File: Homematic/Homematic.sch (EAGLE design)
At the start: 26 parts, among them IC1 3.3V, IC2 3.3V, P1 DF11-06-2DS, Q1 BS170

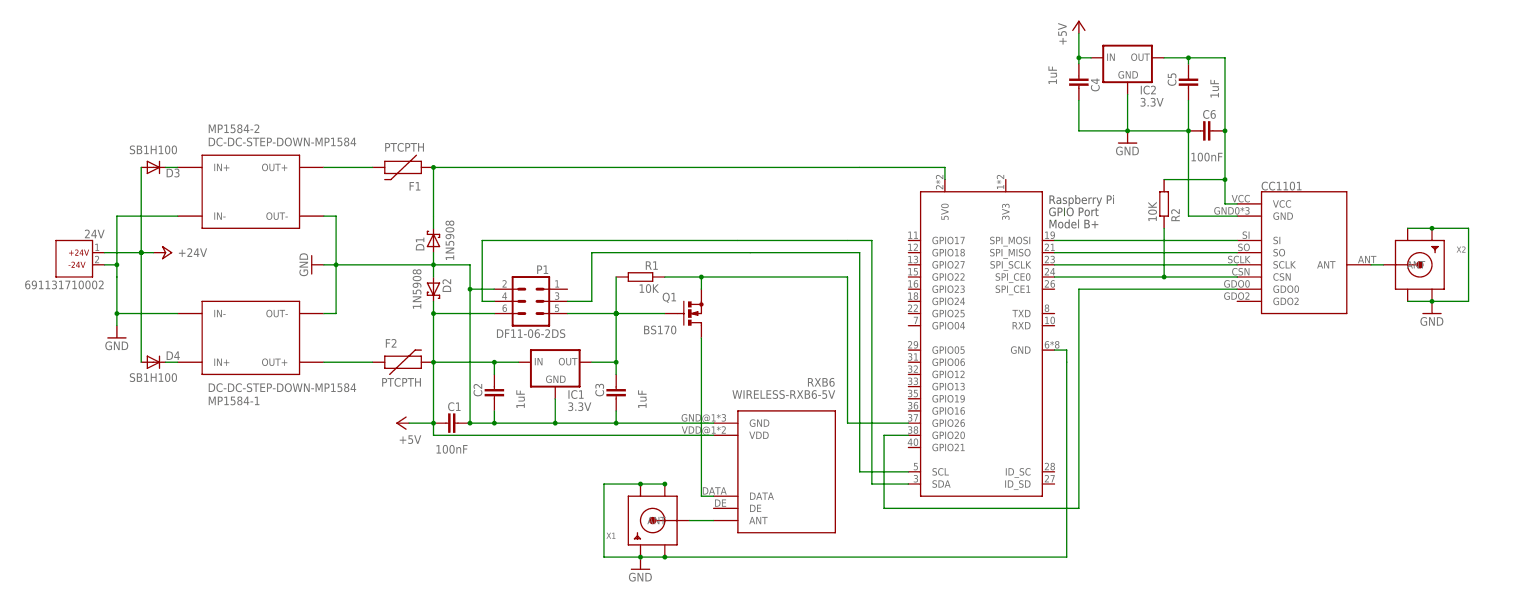
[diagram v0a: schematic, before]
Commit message: Add simple filter for RXB6 data output.
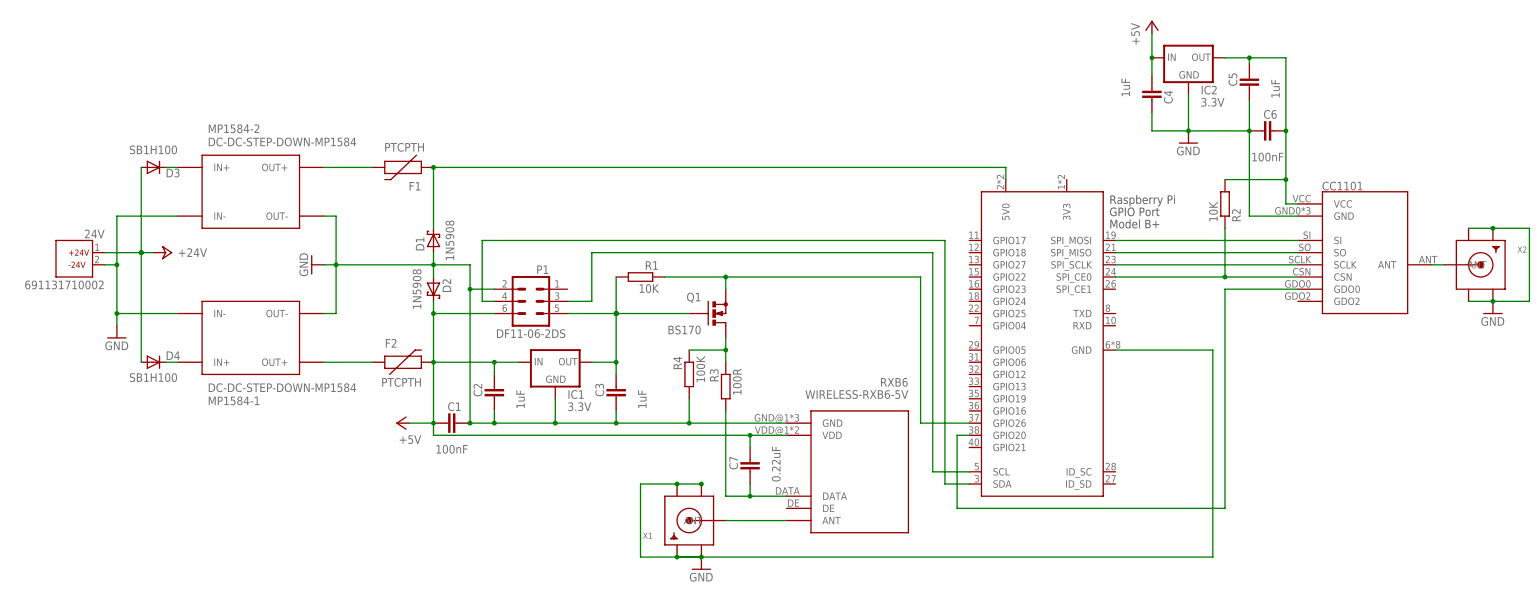
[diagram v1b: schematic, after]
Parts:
- added C7: 0.22uF, capacitor-wima:C2,5-3
- added R3: 100R, rcl:R-EU_0204/2V
- added R4: 100K, rcl:R-EU_0204/5
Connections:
- new net N$2: C7.2, R3.2, RXB6.DATA
- net +5V: now also C7.1
- net GND: now also R4.2
- net N$3: now also R3.1, R4.1; no longer RXB6.DATA
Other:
- moved on the sheet: C4, C5, C6, CC1101, IC2, Q1, R2, RXB6, X1, X2

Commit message: Remove simple filter for RXB6 data output, since no improvement. Change layout and some wires.
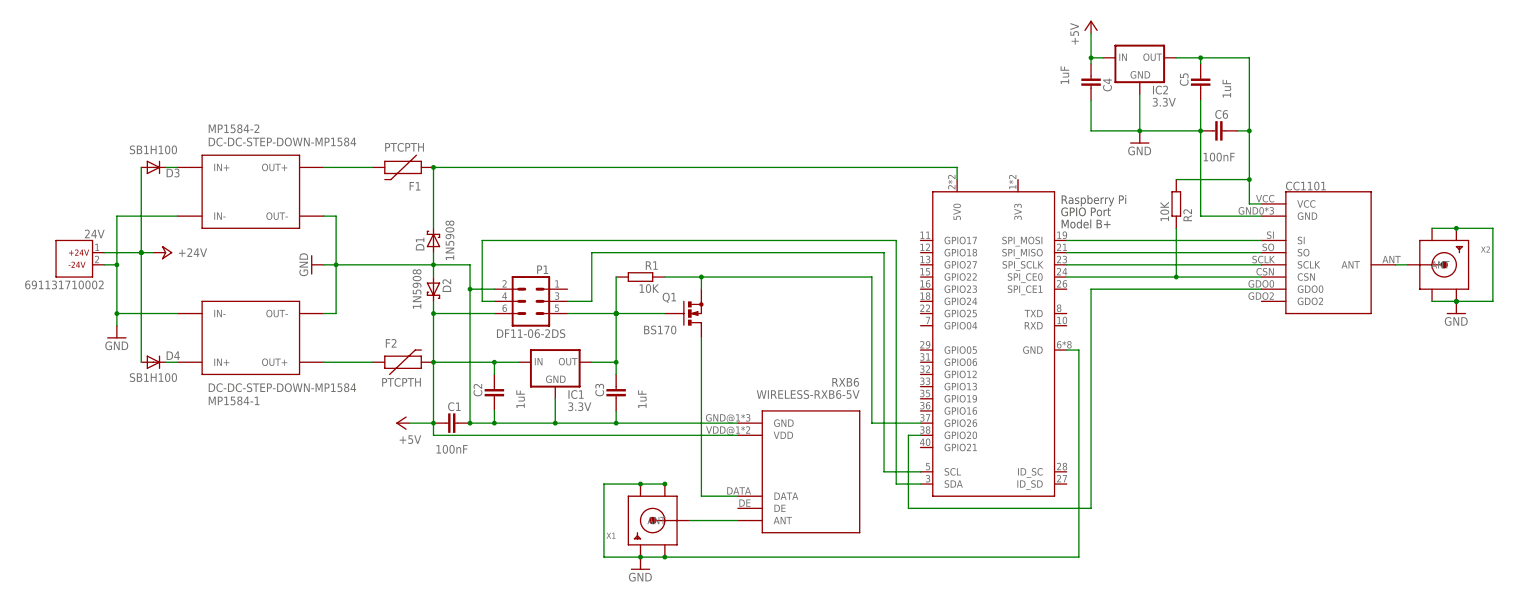
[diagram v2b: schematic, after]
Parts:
- removed C7: 0.22uF, capacitor-wima:C2,5-3
- removed R3: 100R, rcl:R-EU_0204/2V
- removed R4: 100K, rcl:R-EU_0204/5
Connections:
- removed net N$2: C7.2, R3.2, RXB6.DATA
- net +5V: no longer C7.1
- net GND: no longer R4.2
- net N$3: now also RXB6.DATA; no longer R3.1, R4.1
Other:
- moved on the sheet: C4, C5, C6, CC1101, IC2, Q1, R2, RXB6, X1, X2

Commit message: Make Eagle library for used components.
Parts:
- CC1101: device homematic:CC1101 -> modules:CC1101
- MP1584-1, MP1584-2: device diy-modules:DC-DC-STEP-DOWN-MP1584 -> modules:DC-DC-STEP-DOWN-MP1584
- RXB6: device diy-modules:WIRELESS-RXB6-5V -> modules:WIRELESS-RXB6-5V
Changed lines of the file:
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@@
 <attribute name="OC_FARNELL" value="unknown"/>
 </part>
-<part name="MP1584-2" library="diy-modules" deviceset="DC-DC-STEP-DOWN-MP1584" device=""/>
-<part name="MP1584-1" library="diy-modules" deviceset="DC-DC-STEP-DOWN-MP1584" device=""/>
+<part name="MP1584-2" library="modules" deviceset="DC-DC-STEP-DOWN-MP1584" device=""/>
+<part name="MP1584-1" library="modules" deviceset="DC-DC-STEP-DOWN-MP1584" device=""/>
 <part name="D3" library="diode" deviceset="DIODE-" device="DO41-7.6" value="SB1H100"/>
 <part name="D4" library="diode" deviceset="DIODE-" device="DO41-7.6" value="SB1H100"/>
 <part name="C1" library="capacitor-wima" deviceset="C" device="2,5-3" value="100nF"/>
-<part name="RXB6" library="diy-modules" deviceset="WIRELESS-RXB6-5V" device=""/>
+<part name="RXB6" library="modules" deviceset="WIRELESS-RXB6-5V" device=""/>
 <part name="GND3" library="supply1" deviceset="GND" device=""/>
 <part name="IC1" library="adafruit" deviceset="MCP1700" device="TRI" value="3.3V"/>
@@
 <part name="X2" library="adafruit" deviceset="SMACONNECTOR" device=""/>
 <part name="GND4" library="supply1" deviceset="GND" device=""/>
-<part name="CC1101" library="homematic" deviceset="CC1101" device=""/>
+<part name="CC1101" library="modules" deviceset="CC1101" device=""/>
 <part name="IC2" library="adafruit" deviceset="MCP1700" device="TRI" value="3.3V"/>
 <part name="C4" library="capacitor-wima" deviceset="C" device="5/3" value="1uF"/>

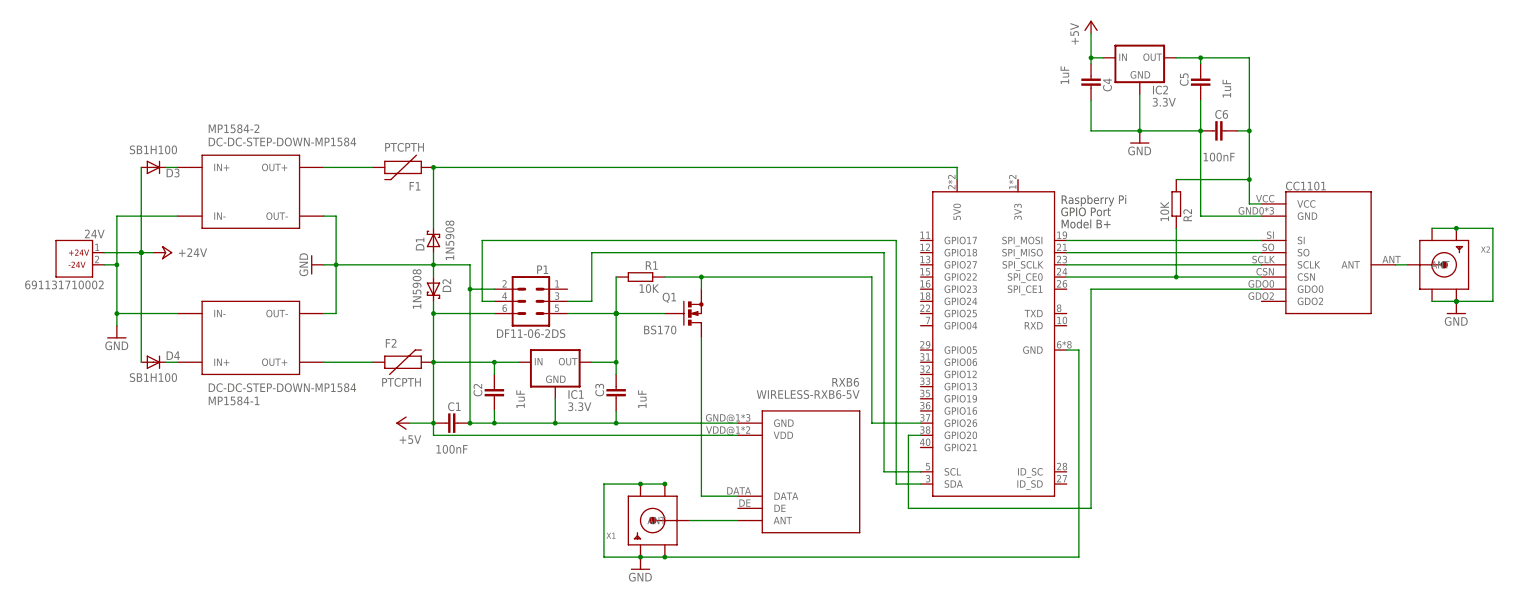
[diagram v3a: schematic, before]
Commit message: Replace RBX6 with RXB8
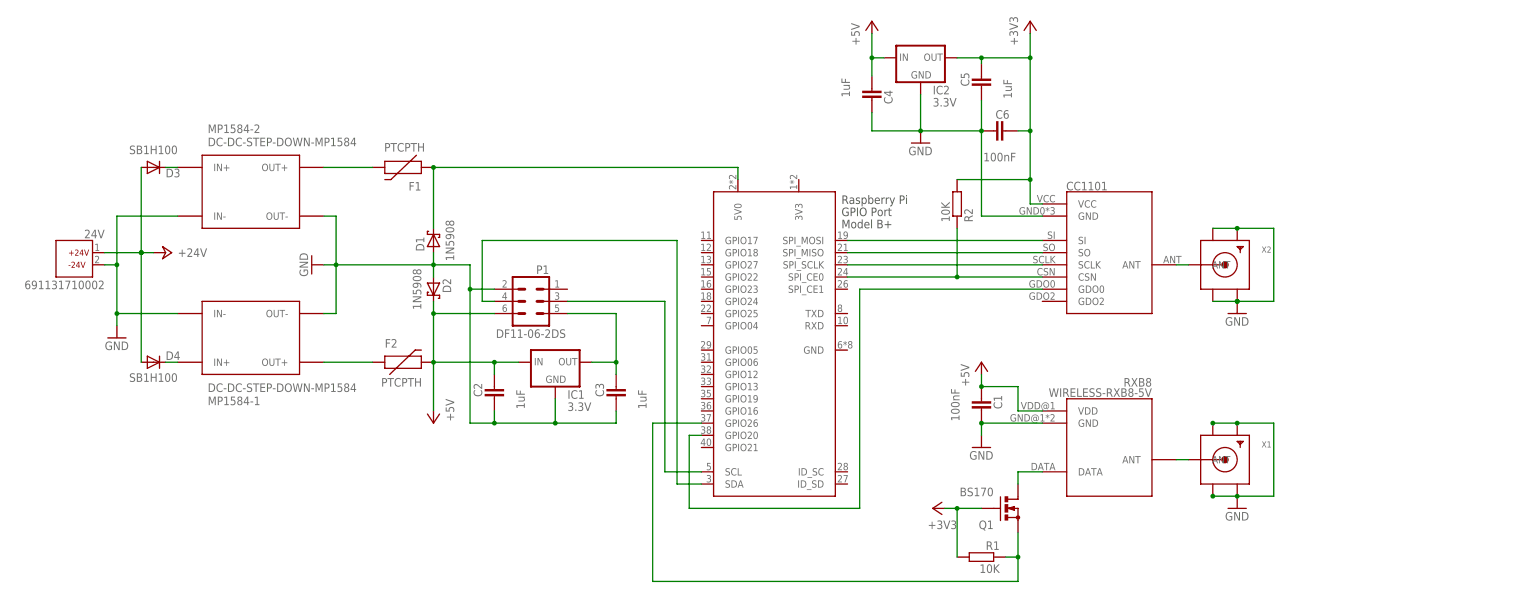
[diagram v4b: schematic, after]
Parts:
- removed RXB6: WIRELESS-RXB6-5V, modules:WIRELESS-RXB6-5V
- added RXB8: WIRELESS-RXB8-5V, modules:WIRELESS-RXB8-5V
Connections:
- removed net N$10: C3.1, IC1.OUT, P1.5, Q1.G, R1.2
- removed net N$11: C5.1, C6.1, CC1101.VCC, IC2.OUT, R2.2
- new net +3V3: C5.1, C6.1, CC1101.VCC, IC2.OUT, Q1.G, R1.2, R2.2
- new net N$2: C3.1, IC1.OUT, P1.5
- net +5V: now also C1.1, RXB8.VDD; no longer C1.2, RXB6.VDD
- net GND: now also C1.2, RXB8.GND; no longer C1.1, RPI.GND, RXB6.GND
- net N$3: now also RXB8.DATA; no longer RXB6.DATA
- net N$8: now also RXB8.ANT; no longer RXB6.ANT
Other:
- moved on the sheet: C1, C4, C5, C6, CC1101, IC2, Q1, R1, R2, X1, X2
